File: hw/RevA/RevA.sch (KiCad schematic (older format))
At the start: 110 parts, among them CON1 N64-Cartridge, J1 USB_C_Receptacle_USB2.0, J2 Micro_SD_Card, J3 DNP Conn_01x02, SW1 SW_Push, U1 SY8120B1ABC, U2 XC6206P25, U3 SY8120B1ABC, U4 SPI Flash W25Q128JVSIQ, U6 IS42S16320F-7TL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

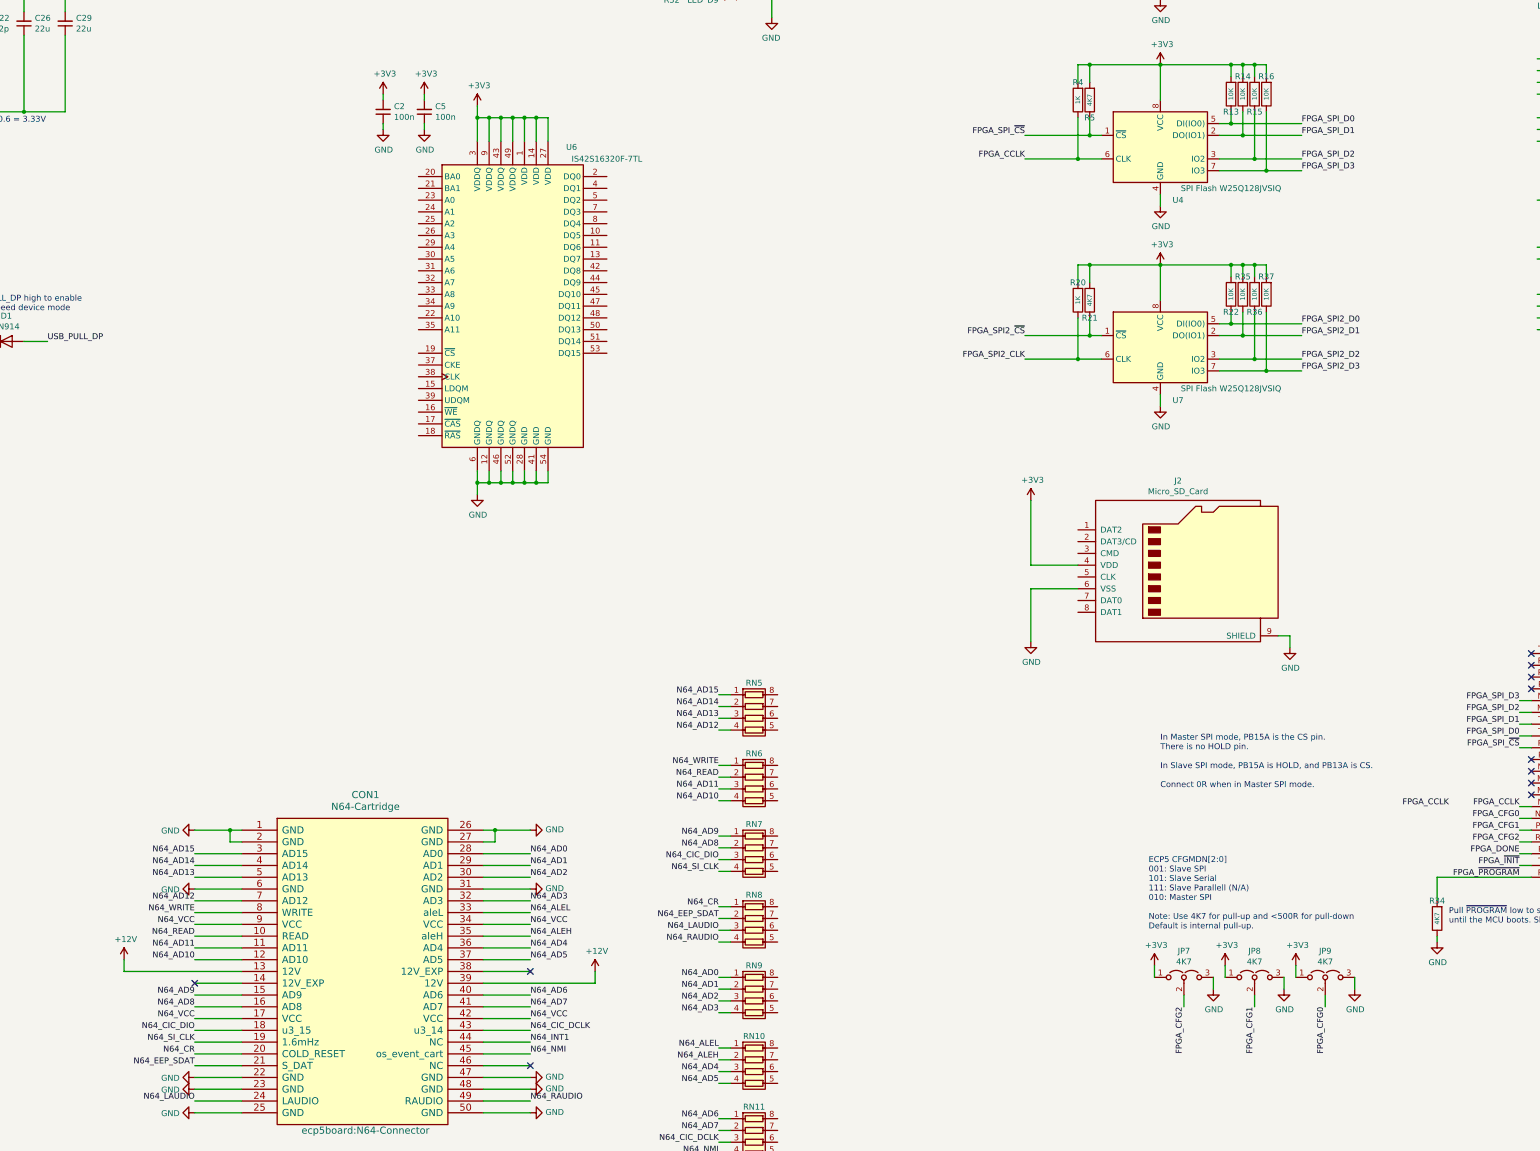
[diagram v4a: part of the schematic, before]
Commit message: hw: Progress
- Added pullup resistor for CIC data
- Removed extra SPI flash (no need for it anymore)
- Rounded corners
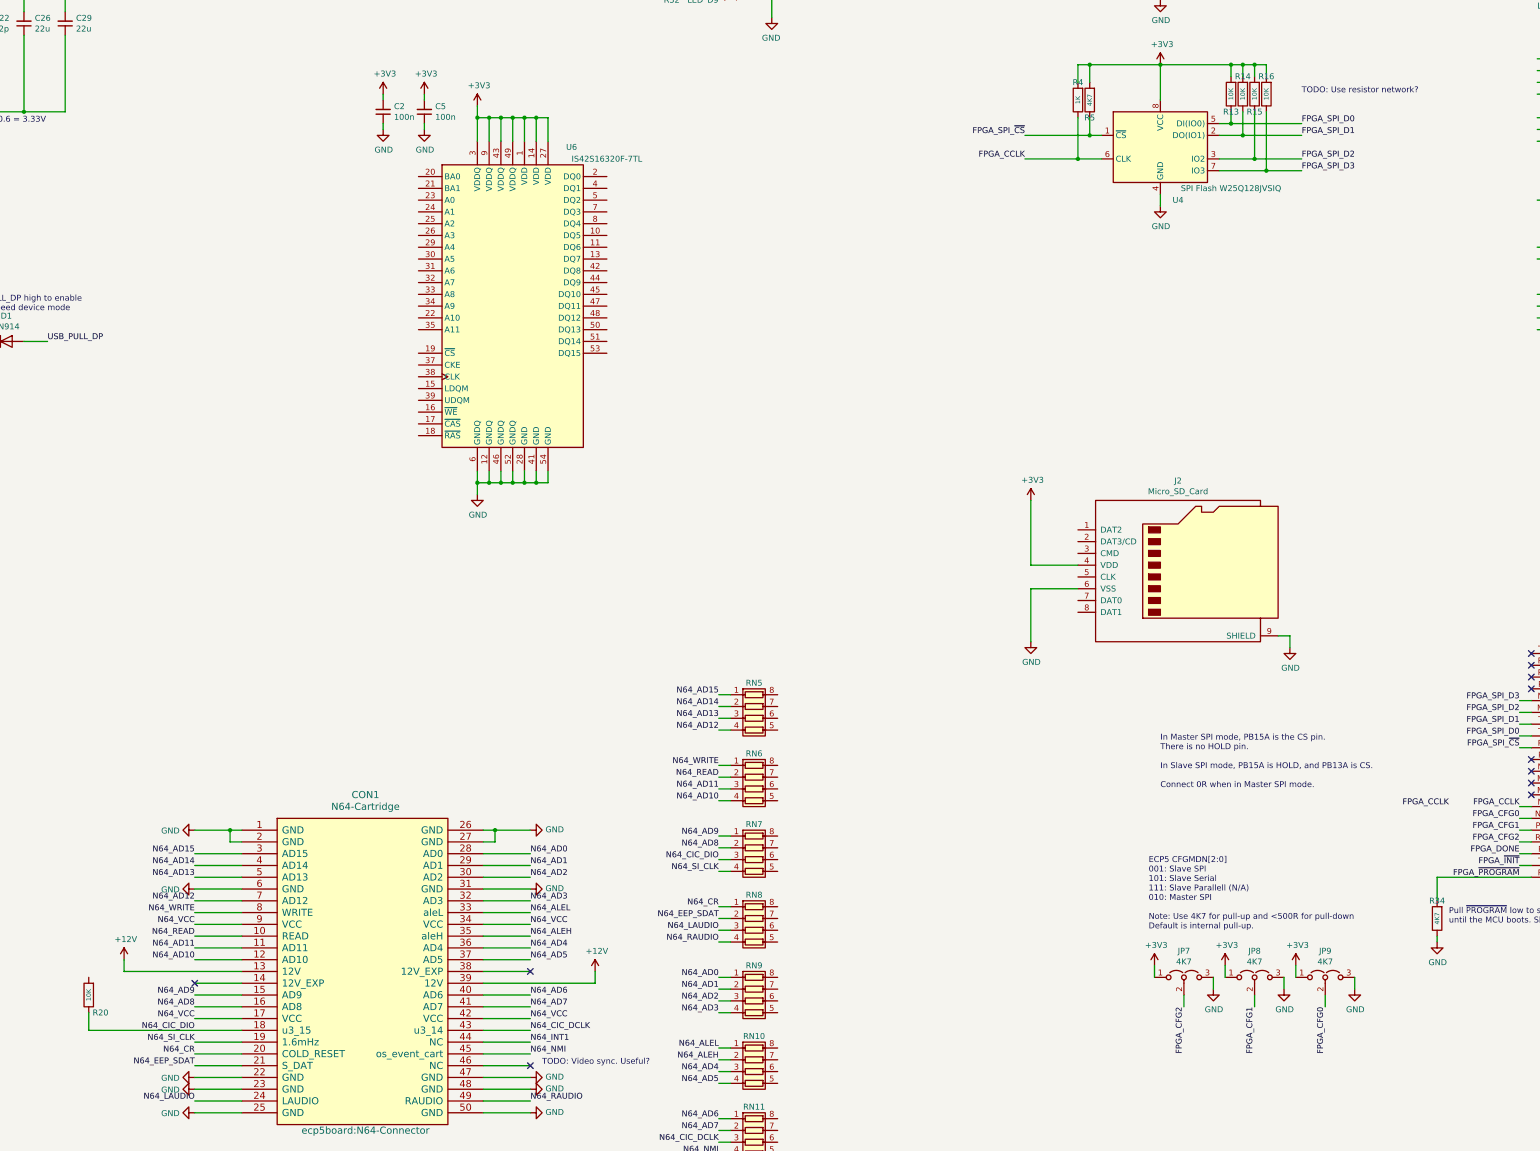
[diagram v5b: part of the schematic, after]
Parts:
- removed R21: 4K7, Resistor_SMD:R_0402_1005Metric, symbol Device:R
- removed R22, R35, R36, R37: 10K, Resistor_SMD:R_0402_1005Metric, symbol Device:R
- removed U7: SPI Flash W25Q128JVSIQ, ecp5board:SOA008-150-208mil, symbol Memory_Flash:W25Q32JVSS
- R20: value 1K -> 10K
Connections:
- net labels removed: FPGA_SPI2_CLK, FPGA_SPI2_D0, FPGA_SPI2_D1, FPGA_SPI2_D2, FPGA_SPI2_D3, FPGA_SPI2_~CS~
- wire segments 678 -> 647
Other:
- note added: "TODO: Use resistor network?"
- note added: "TODO: Video sync. Useful?"
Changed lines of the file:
@@
 Wire Wire Line
 	12700 10500 13100 10500
-Wire Wire Line
-	12650 8550 13100 8550
-Text Label 12650 8350 2    50   ~ 0
-FPGA_SPI2_~CS~
-Text Label 12650 8550 2    50   ~ 0
-FPGA_SPI2_CLK
-Text Label 15000 8650 0    50   ~ 0
-FPGA_SPI2_D3
-Text Label 15000 8550 0    50   ~ 0
-FPGA_SPI2_D2
-Text Label 15000 8350 0    50   ~ 0
-FPGA_SPI2_D1
-Text Label 15000 8250 0    50   ~ 0
-FPGA_SPI2_D0
-$Comp
-L Device:R R21
-U 1 1 6282AA8A
-P 13200 8050
-F 0 "R21" H 13200 8200 50  0000 C CNN
-F 1 "4K7" V 13200 8050 39  0000 C CNN
-F 2 "Resistor_SMD:R_0402_1005Metric" V 13130 8050 50  0001 C CNN
-F 3 " " H 13200 8050 50  0001 C CNN
-	1    13200 8050
-	-1   0    0    1
-$EndComp
-Wire Wire Line
-	13800 7750 13800 8050
-$Comp
-L power:+3V3 #PWR0117
-U 1 1 6282AA91
-P 13800 7750
-F 0 "#PWR0117" H 13800 7600 50  0001 C CNN
-F 1 "+3V3" H 13815 7923 50  0000 C CNN
-F 2 "" H 13800 7750 50  0001 C CNN
-F 3 "" H 13800 7750 50  0001 C CNN
-	1    13800 7750
-	1    0    0    -1
-$EndComp
-Wire Wire Line
-	13800 8950 13800 8850
-$Comp
-L power:GND #PWR0118
-U 1 1 6282AA98
-P 13800 8950
-F 0 "#PWR0118" H 13800 8700 50  0001 C CNN
-F 1 "GND" H 13805 8777 50  0000 C CNN
-F 2 "" H 13800 8950 50  0001 C CNN
-F 3 "" H 13800 8950 50  0001 C CNN
-	1    13800 8950
-	1    0    0    -1
-$EndComp
-$Comp
-L Memory_Flash:W25Q32JVSS U7
-U 1 1 6282AAA1
-P 13800 8450
-F 0 "U7" H 13950 8000 50  0000 C CNN
-F 1 "SPI Flash W25Q128JVSIQ" H 14400 8100 50  0000 C CNN
-F 2 "ecp5board:SOA008-150-208mil" H 13800 8450 50  0001 C CNN
-F 3 "https://datasheet.lcsc.com/szlcsc/1811142111_Winbond-Elec-W25Q128JVSIQ_C97521.pdf" H 13800 8450 50  0001 C CNN
-F 4 "C97521" H 13800 8450 50  0001 C CNN "LCSC"
-F 5 "https://lcsc.com/product-detail/FLASH_Winbond-Elec-W25Q128JVSIQTR_C97521.html" H 13800 8450 50  0001 C CNN "LCSC URL"
-F 6 "0.4692" H 13800 8450 50  0001 C CNN "LCSC EUR"
-	1    13800 8450
-	1    0    0    -1
-$EndComp
-Connection ~ 13200 8350
-Wire Wire Line
-	13200 8350 13300 8350
-Wire Wire Line
-	13200 8350 13200 8200
-Wire Wire Line
-	12650 8350 13200 8350
-$Comp
-L Device:R R20
-U 1 1 6282AAAB
-P 13100 8050
-F 0 "R20" H 13100 7900 50  0000 C CNN
-F 1 "1K" V 13100 8050 39  0000 C CNN
-F 2 "Resistor_SMD:R_0402_1005Metric" V 13030 8050 50  0001 C CNN
-F 3 " " H 13100 8050 50  0001 C CNN
-	1    13100 8050
-	-1   0    0    1
-$EndComp
-Wire Wire Line
-	13100 8200 13100 8550
-Connection ~ 13100 8550
-Wire Wire Line
-	13100 8550 13300 8550
-Wire Wire Line
-	14500 7750 14500 7850
-$Comp
-L Device:R R35
-U 1 1 6282AAB5
-P 14500 8000
-F 0 "R35" H 14500 7850 50  0000 C CNN
-F 1 "10K" V 14500 8000 39  0000 C CNN
-F 2 "Resistor_SMD:R_0402_1005Metric" V 14430 8000 50  0001 C CNN
-F 3 " " H 14500 8000 50  0001 C CNN
-	1    14500 8000
-	-1   0    0    1
-$EndComp
-Wire Wire Line
-	14400 7750 14400 7850
-$Comp
-L Device:R R22
-U 1 1 6282AABC
-P 14400 8000
-F 0 "R22" H 14400 8150 50  0000 C CNN
-F 1 "10K" V 14400 8000 39  0000 C CNN
-F 2 "Resistor_SMD:R_0402_1005Metric" V 14330 8000 50  0001 C CNN
-F 3 " " H 14400 8000 50  0001 C CNN
-	1    14400 8000
-	-1   0    0    1
-$EndComp
-Wire Wire Line
-	14700 7750 14700 7850
-$Comp
-L Device:R R37
-U 1 1 6282AAC3
-P 14700 8000
-F 0 "R37" H 14700 7850 50  0000 C CNN
-F 1 "10K" V 14700 8000 39  0000 C CNN
-F 2 "Resistor_SMD:R_0402_1005Metric" V 14630 8000 50  0001 C CNN
-F 3 " " H 14700 8000 50  0001 C CNN
-	1    14700 8000
-	-1   0    0    1
-$EndComp
-Wire Wire Line
-	14600 7750 14600 7850
-$Comp
-L Device:R R36
-U 1 1 6282AACA
-P 14600 8000
-F 0 "R36" H 14600 8150 50  0000 C CNN
-F 1 "10K" V 14600 8000 39  0000 C CNN
-F 2 "Resistor_SMD:R_0402_1005Metric" V 14530 8000 50  0001 C CNN
-F 3 " " H 14600 8000 50  0001 C CNN
-	1    14600 8000
-	-1   0    0    1
-$EndComp
-Wire Wire Line
-	14300 8250 14400 8250
-Wire Wire Line
-	14300 8350 14500 8350
-Wire Wire Line
-	14300 8550 14600 8550
-Wire Wire Line
-	14300 8650 14700 8650
-Wire Wire Line
-	14400 8150 14400 8250
-Connection ~ 14400 8250
-Wire Wire Line
-	14400 8250 15000 8250
-Wire Wire Line
-	14500 8150 14500 8350
-Connection ~ 14500 8350
-Wire Wire Line
-	14500 8350 15000 8350
-Wire Wire Line
-	14600 8150 14600 8550
-Connection ~ 14600 8550
-Wire Wire Line
-	14600 8550 15000 8550
-Wire Wire Line
-	14700 8150 14700 8650
-Connection ~ 14700 8650
-Wire Wire Line
-	14700 8650 15000 8650
-Wire Wire Line
-	14700 7750 14600 7750
-Wire Wire Line
-	13200 7750 13200 7900
-Connection ~ 13800 7750
-Wire Wire Line
-	13800 7750 13200 7750
-Connection ~ 14400 7750
-Wire Wire Line
-	14400 7750 13800 7750
-Connection ~ 14500 7750
-Wire Wire Line
-	14500 7750 14400 7750
-Connection ~ 14600 7750
-Wire Wire Line
-	14600 7750 14500 7750
-Wire Wire Line
-	13200 7750 13100 7750
-Wire Wire Line
-	13100 7750 13100 7900
-Connection ~ 13200 7750
 $Comp
 L Memory_RAM:IS42S16400J-xC U6
@@
 Wire Wire Line
 	5600 14150 6000 14150
-Wire Wire Line
-	5600 14250 6000 14250
 Wire Wire Line
 	5600 14350 6000 14350
@@
 Text Label 8450 14350 0    50   ~ 0
 N64_INT1
+$Comp
+L Device:R R20
+U 1 1 613DD002
+P 4700 13950
+F 0 "R20" H 4600 14100 50  0000 C CNN
+F 1 "10K" V 4700 13950 39  0000 C CNN
+F 2 "Resistor_SMD:R_0402_1005Metric" V 4630 13950 50  0001 C CNN
+F 3 " " H 4700 13950 50  0001 C CNN
+	1    4700 13950
+	-1   0    0    1
+$EndComp
+Wire Wire Line
+	4700 14250 4700 14100
+Wire Wire Line
+	4700 14250 6000 14250
+Text Notes 8550 14550 0    50   ~ 0
+TODO: Video sync. Useful?
+Text Notes 15000 6300 0    50   ~ 0
+TODO: Use resistor network?
 $EndSCHEMATC
